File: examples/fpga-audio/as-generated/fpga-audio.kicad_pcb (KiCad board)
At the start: 4 copper layers, 76 x 58 mm, 36 parts, among them J1 3V3 IN, J2 AUDIO OUT, J3 SPI PROG, U1 iCE40UP5K, U2 PCM5102A, U3 AP2112K-1.2, U4 W25Q32JV, X1 12MHz

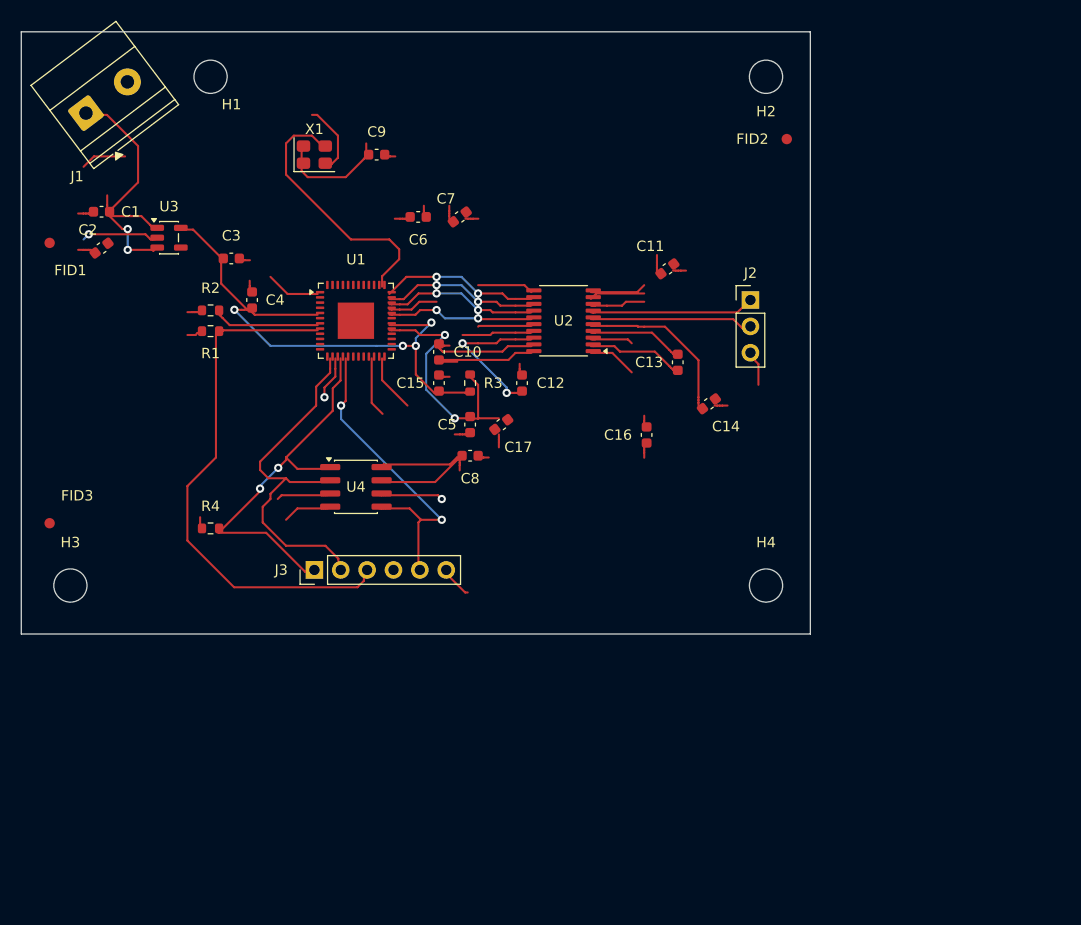
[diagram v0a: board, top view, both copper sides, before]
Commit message: feat(examples): the FPGA board on two layers, and the rim fenced in the generator
The last of the five, and the one that had to be re-floorplanned rather than
converted: a 48-pin QFN, a codec, a boot flash and an oscillator escaped on two
faces. All five examples are now two-layer and gate clean.

What moved, and why:

* the boot flash came up ten millimetres to meet the FPGA's SPI port, the
  configuration header eight west along the bottom edge it serves, and CRESET's
  pull-up now stands between its two ends instead of beside CDONE's. Together
  those took `layout.connection_span` from nine findings - worst 51.5 mm - to
  the four I2S runs at 25.7 mm, which are the two packages' own width.
* the outer ring of the pour is now a router keepout, not just something the
  review reports afterwards. On the widest board in the set the perimeter is
  the emptiest lane there is and the router took it twice, for 20.5 mm of the
  bottom edge and 11.5 mm of the right. Reporting that is `layout.pour_edge_cut`;
  not building it is the generator's job.
* the input rail goes round the screw terminal rather than under its body, the
  core rail's link to its spine is asked for at the width it lands on, and the
  oscillator's bypass takes its supply from the neighbour eight millimetres
  away instead of the flash's bypass fifty-two millimetres away.

What is judged rather than fixed is in `gate.toml` with its measurements: the
two-layer return path on the SPI bus, XSMT's detour - R6 in the corridor was
tried and left five nets with no lane at all - the I2S spans, and two marginal
router artifacts on one escape.

Co-Authored-By: Claude Opus 5 <noreply@anthropic.com>
Claude-Session: https://claude.ai/code/session_01XQE7UkE9WTSMW3oZ3kLeCt
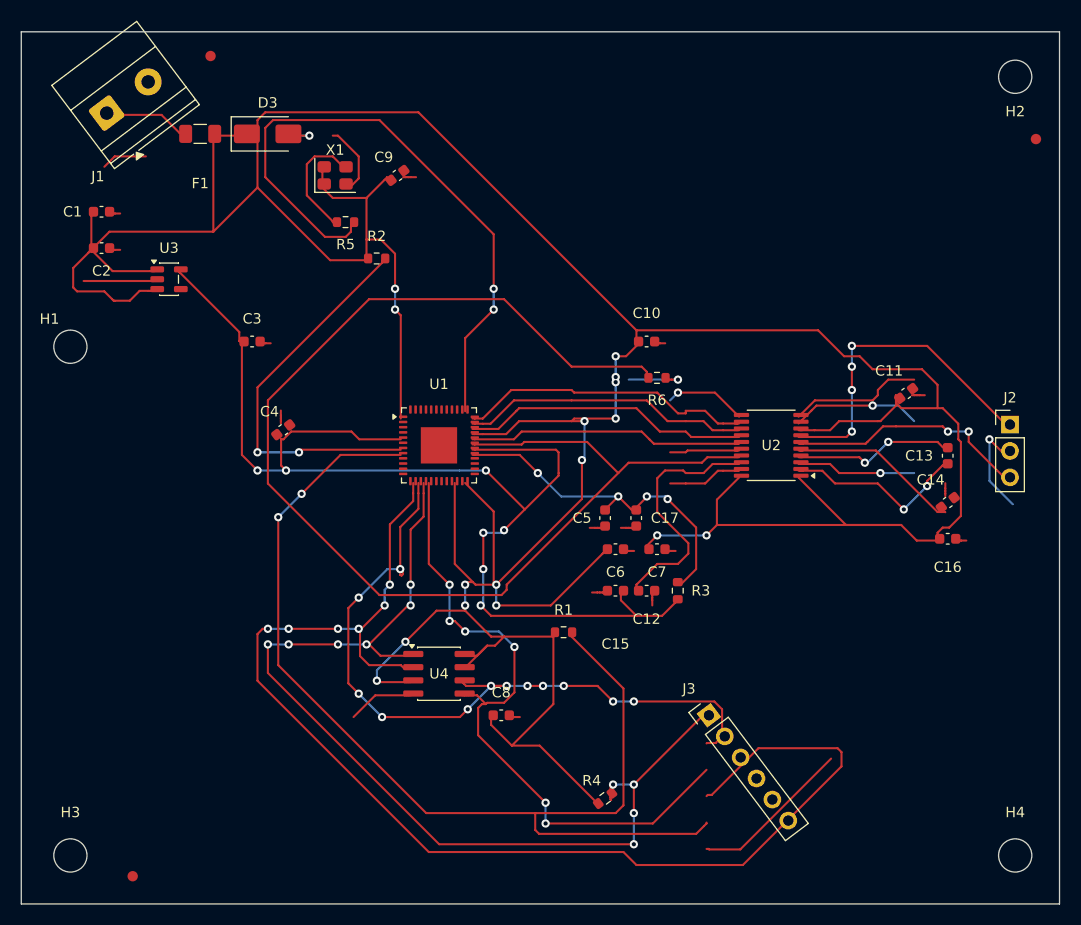
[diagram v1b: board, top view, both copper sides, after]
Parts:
- added C2: 100n, Capacitor_SMD:C_0603_1608Metric, F.Cu at (107.7, 80.8)
- added D3: SMAJ5.0A, Diode_SMD:D_SMA, F.Cu at (123.7, 69.8)
- added R5: 33R, Resistor_SMD:R_0603_1608Metric, F.Cu at (131.2, 78.3)
- added R6: 10k, Resistor_SMD:R_0603_1608Metric, F.Cu at (161.2, 93.3)
- F1: renamed from C2; value 100n -> 500mA; footprint Capacitor_SMD:C_0603_1608Metric -> Fuse:Fuse_1206_3216Metric
- moved R4 46.0 mm to (156.2, 133.8), turned to 37 degrees
- moved R1 44.7 mm to (152.2, 117.8)
- moved J3 40.5 mm to (166.2, 125.8), turned to 37 degrees
- moved C6 37.2 mm to (157.2, 109.8), turned to 0 degrees
- moved C7 37.2 mm to (161.2, 109.8), turned to 0 degrees
- moved H4 35.4 mm to (195.7, 139.3)
- moved FID3 34.9 mm to (110.7, 141.3)
- moved C16 30.7 mm to (189.2, 108.8), turned to 0 degrees
- moved H1 29.3 mm to (104.7, 90.3)
- moved R3 28.3 mm to (163.2, 113.8)
- moved J2 27.7 mm to (195.2, 97.8)
- moved C13 27.5 mm to (189.2, 100.8)
- moved C15 26.2 mm to (157.2, 113.8), turned to 180 degrees
- moved H3 26.0 mm to (104.7, 139.3)
- moved C11 25.9 mm to (185.2, 94.8)
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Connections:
- F1 pad 1: +3V3 -> /VIN
- F1 pad 2: GND -> +3V3
- J1 pad 1: +3V3 -> /VIN
- J2 pad 2: /OUTL -> GND
- J2 pad 3: GND -> /OUTL
- J3 pad 2: /SPI_SO -> /SPI_SCK
- J3 pad 3: /CRESET -> /SPI_SI
- J3 pad 4: /SPI_SCK -> /SPI_SO
- J3 pad 5: /SPI_SI -> /CRESET
- U1 pad 31: unconnected-(U1A-IOT_42b-Pad31) -> /XSMT
- U2 pad 17: +3V3 -> /XSMT
- X1 pad 3: /CLK12 -> /OSC_OUT
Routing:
- net +3V3: track 122.1 -> 412.4 mm, vias 2 -> 16
- net /XSMT: track 0.00 -> 123.2 mm
- net /SPI_SO: track 35.7 -> 122.8 mm, vias 0 -> 6
- net /+1V2: track 54.2 -> 115.0 mm, vias 4 -> 7
- net /SPI_SS: track 37.0 -> 96.2 mm, vias 2 -> 10
- net GND: track 83.4 -> 137.8 mm, vias 1 -> 6
- net /CRESET: track 51.2 -> 105.4 mm, vias 0 -> 2
- net /SPI_SCK: track 34.7 -> 72.6 mm, vias 2 -> 12
- net /CLK12: track 25.6 -> 61.4 mm, vias 0 -> 2
- net /SPI_SI: track 31.4 -> 64.0 mm, vias 2 -> 6
- net /CDONE: track 10.2 -> 37.4 mm, vias 0 -> 2
- net /OUTR: track 15.6 -> 31.8 mm, vias 0 -> 4
- net /I2S_SCK: track 15.3 -> 28.5 mm, vias 2 -> 0
- net /I2S_DIN: track 14.9 -> 27.7 mm, vias 2 -> 0
- net /I2S_BCK: track 15.1 -> 27.8 mm, vias 2 -> 0
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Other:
- board size 76 x 58 mm -> 100 x 84 mm
- copper layers 4 -> 2

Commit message: fix(examples): merge same-net vias a drill cannot place that close
The FPGA board's move to two layers put every layer change on the same
pair of faces, and the search spends a via at each end of a hop. Two hops
that turned round within half a millimetre of each other got a barrel
apiece: 0.5 mm between centres, 0.1 mm between the holes, against the
0.2495 mm the board setup allows. KiCad's DRC reported hole_to_hole; the
gate did not, because the constraint is the board setup's rather than a
rule this toolkit writes.

The pair is one hole on one net whose copper already overlaps. `_uncrowded`
runs after the copper has stopped moving, finds same-net vias closer than
HOLE_TO_HOLE_MM, and puts one via at the centre of every track end the two
were serving - only if that one still reaches all of them. A pad-anchored
via never moves.

Also renumber the two REVIEW.md sections that both came out of the merge
as 26.

Co-Authored-By: Claude Opus 5 <noreply@anthropic.com>
Claude-Session: https://claude.ai/code/session_01XQE7UkE9WTSMW3oZ3kLeCt
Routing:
- net +3V3: vias 16 -> 15
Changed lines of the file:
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@@
   )
   (via
-    (at 163.25 94.75)
+    (at 182 96)
     (size 0.8)
     (drill 0.4)
@@
   )
   (via
-    (at 182 96)
+    (at 182.75 102.5)
     (size 0.8)
     (drill 0.4)
@@
   )
   (via
-    (at 182.75 102.5)
+    (at 193.25 99.25)
     (size 0.8)
     (drill 0.4)
@@
   )
   (via
-    (at 193.25 99.25)
+    (at 163.25 93.5)
     (size 0.8)
     (drill 0.4)
@@
   )
   (via
-    (at 163.25 93.5)
+    (at 163.25 94.75)
     (size 0.8)
     (drill 0.4)
@@
   )
   (via
-    (at 161.25 108.5)
+    (at 166 108.5)
     (size 0.8)
     (drill 0.4)
@@
   )
   (via
-    (at 157.25 93.75)
-    (size 0.8)
-    (drill 0.4)
-    (layers "F.Cu" "B.Cu")
-    (net 3)
-  )
-  (via
-    (at 166 108.5)
+    (at 157.25 97.25)
     (size 0.8)
     (drill 0.4)
@@
   )
   (via
-    (at 157.25 93.25)
+    (at 157.25 93.5)
     (size 0.8)
     (drill 0.4)
@@
   )
   (via
-    (at 157.25 97.25)
+    (at 161.25 108.5)
     (size 0.8)
     (drill 0.4)
@@
   )
   (via
-    (at 183.5 99.5)
+    (at 181.25 101.5)
     (size 0.8)
     (drill 0.4)
@@
   )
   (via
-    (at 181.25 101.5)
+    (at 183.5 99.5)
     (size 0.8)
     (drill 0.4)
@@
   )
   (via
-    (at 145.5 86.75)
+    (at 145.5 84.75)
     (size 0.8)
     (drill 0.4)
@@
   )
   (via
-    (at 145.5 84.75)
+    (at 145.5 86.75)
     (size 0.8)
     (drill 0.4)
@@
   )
   (via
-    (at 124.75 106.75)
+    (at 127 104.5)
     (size 0.8)
     (drill 0.4)
@@
   )
   (via
-    (at 127 104.5)
+    (at 124.75 106.75)
     (size 0.8)
     (drill 0.4)
@@
   )
   (via
-    (at 191.25 98.5)
+    (at 189.25 98.5)
     (size 0.8)
     (drill 0.4)
@@
   )
   (via
-    (at 189.25 98.5)
+    (at 191.25 98.5)
     (size 0.8)
     (drill 0.4)
@@
   )
   (via
-    (at 180 90.25)
+    (at 180 92.25)
     (size 0.8)
     (drill 0.4)
@@
   )
   (via
-    (at 180 94.5)
+    (at 180 90.25)
     (size 0.8)
     (drill 0.4)
@@
   )
   (via
-    (at 180 92.25)
+    (at 180 94.5)
     (size 0.8)
     (drill 0.4)
@@
   )
   (via
-    (at 146.75 123)
+    (at 148.75 123)
     (size 0.8)
     (drill 0.4)
@@
   )
   (via
-    (at 132.5 114.5)
+    (at 132.5 123.75)
     (size 0.8)
     (drill 0.4)
@@
   )
   (via
-    (at 148.75 123)
+    (at 150.25 123)
     (size 0.8)
     (drill 0.4)
@@
   )
   (via
-    (at 159 124.5)
+    (at 157 124.5)
     (size 0.8)
     (drill 0.4)
@@
   )
   (via
-    (at 150.25 123)
+    (at 136.5 111.75)
     (size 0.8)
     (drill 0.4)
@@
   )
   (via
-    (at 132.5 123.75)
+    (at 159 124.5)
     (size 0.8)
     (drill 0.4)
@@
   )
   (via
-    (at 157 124.5)
+    (at 132.5 114.5)
     (size 0.8)
     (drill 0.4)
@@
   )
   (via
-    (at 136.5 111.75)
+    (at 143 125.25)
     (size 0.8)
     (drill 0.4)
@@
   )
   (via
-    (at 145.25 123)
+    (at 146.75 123)
     (size 0.8)
     (drill 0.4)
@@
   )
   (via
-    (at 143 125.25)
+    (at 145.25 123)
     (size 0.8)
     (drill 0.4)
@@
   )
   (via
-    (at 150.5 134.25)
+    (at 141.25 113.25)
     (size 0.8)
     (drill 0.4)
@@
   )
   (via
-    (at 141.25 116.75)
+    (at 150.5 136.25)
     (size 0.8)
     (drill 0.4)
@@
   )
   (via
-    (at 147.5 119.25)
+    (at 142.75 117.75)
     (size 0.8)
     (drill 0.4)
@@
   )
   (via
-    (at 141.25 113.25)
+    (at 150.5 134.25)
     (size 0.8)
     (drill 0.4)
@@
   )
   (via
-    (at 142.75 117.75)
+    (at 141.25 116.75)
     (size 0.8)
     (drill 0.4)
@@
   )
   (via
-    (at 150.5 136.25)
+    (at 147.5 119.25)
     (size 0.8)
     (drill 0.4)
@@
   )
   (via
-    (at 132.5 117.5)
+    (at 135 115.25)
     (size 0.8)
     (drill 0.4)
@@
   )
   (via
-    (at 135 115.25)
+    (at 132.5 117.5)
     (size 0.8)
     (drill 0.4)
@@
   )
   (via
-    (at 159 132.5)
+    (at 159 135.25)
     (size 0.8)
     (drill 0.4)
@@
   )
   (via
-    (at 125.75 119)
+    (at 130.5 119)
     (size 0.8)
     (drill 0.4)
@@
   )
   (via
-    (at 137.5 113.25)
+    (at 123.75 119)
     (size 0.8)
     (drill 0.4)
@@
   )
   (via
-    (at 159 138.25)
+    (at 137.5 115.25)
     (size 0.8)
     (drill 0.4)
@@
   )
   (via
-    (at 137.5 115.25)
+    (at 157 132.5)
     (size 0.8)
     (drill 0.4)
@@
   )
   (via
-    (at 133.25 119)
+    (at 137.5 113.25)
     (size 0.8)
     (drill 0.4)
@@
   )
   (via
-    (at 159 135.25)
+    (at 159 138.25)
     (size 0.8)
     (drill 0.4)
@@
   )
   (via
-    (at 130.5 119)
+    (at 133.25 119)
     (size 0.8)
     (drill 0.4)
@@
   )
   (via
-    (at 123.75 119)
+    (at 125.75 119)
     (size 0.8)
     (drill 0.4)
@@
   )
   (via
-    (at 157 132.5)
+    (at 159 132.5)
     (size 0.8)
     (drill 0.4)
@@
   )
   (via
-    (at 157.5 104.75)
+    (at 160.25 104.75)
     (size 0.8)
     (drill 0.4)
@@
   )
   (via
-    (at 160.25 104.75)
+    (at 157.5 104.75)
     (size 0.8)
     (drill 0.4)

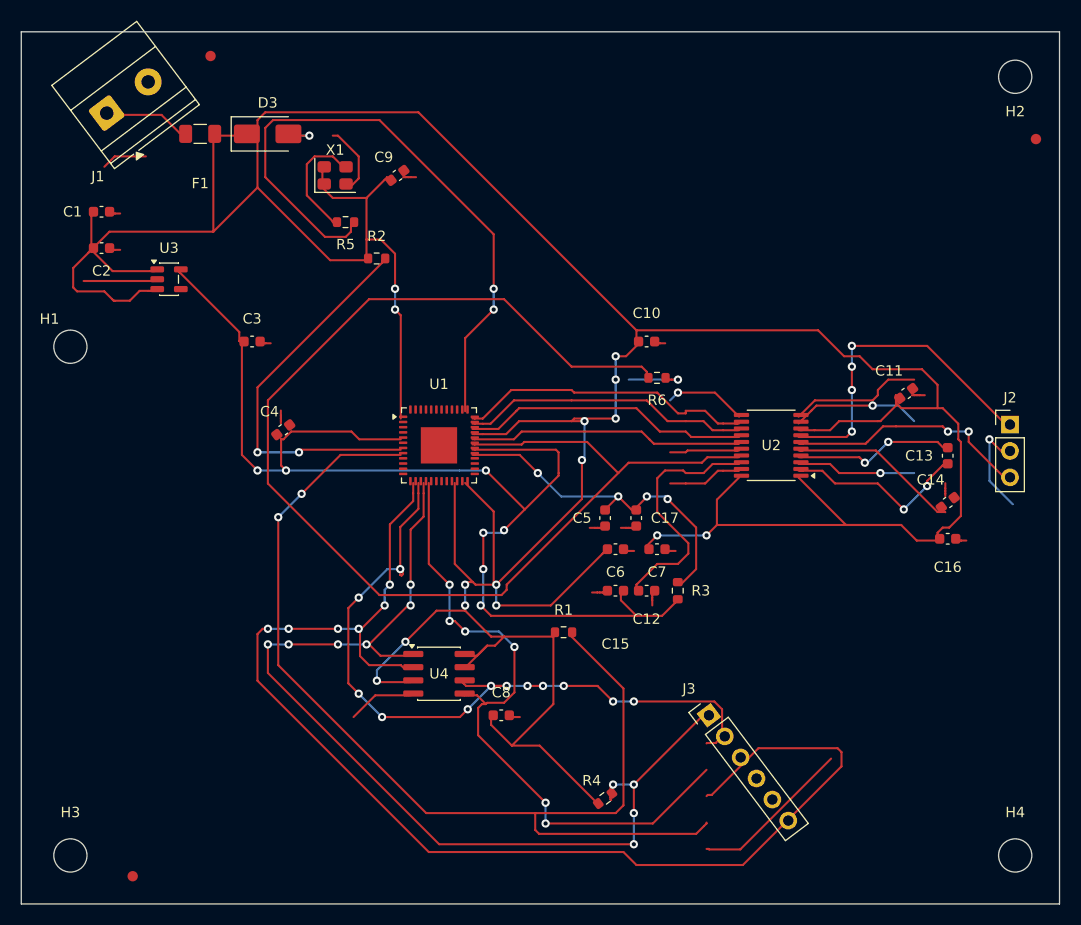
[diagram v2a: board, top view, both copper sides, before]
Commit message: chore(examples): regenerate the FPGA board from a cold route
The board this checkout held came from a warm cache and was clean by
luck: CI routes with an empty cache and no learned rip-up order, found a
different valid solution, and put +3V3 under both headers. With J2 and J3
fenced by body_keepout, the cold route goes round them - no
route.under_package, no pour_edge_cut, DRC clean, gate and contracts pass
on all five boards.

Record the round in REVIEW.md, and state the rule in AGENTS.md: the
copper checked in has to be what a cold route finds, because that is what
the drift check compares against.

Co-Authored-By: Claude Opus 5 <noreply@anthropic.com>
Claude-Session: https://claude.ai/code/session_01XQE7UkE9WTSMW3oZ3kLeCt
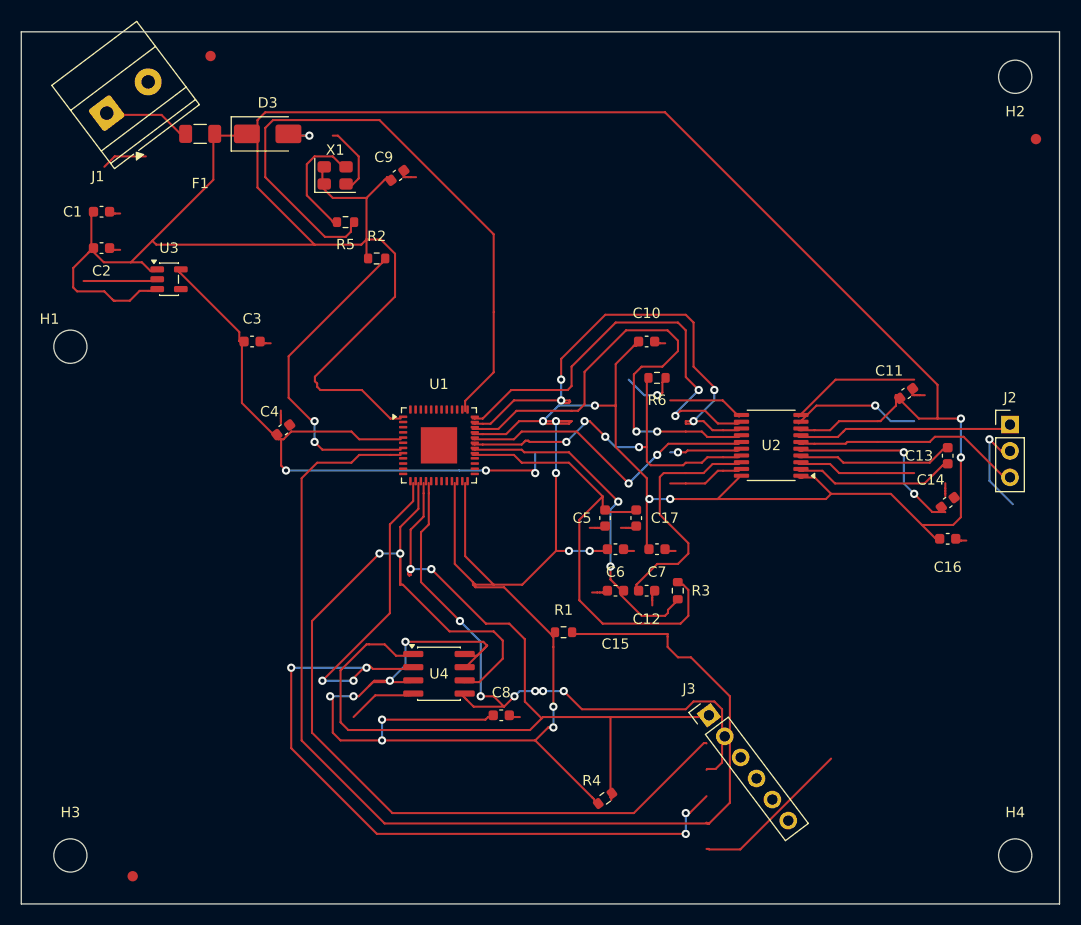
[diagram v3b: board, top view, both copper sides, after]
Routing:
- net /XSMT: track 123.2 -> 36.3 mm, vias 0 -> 4
- net +3V3: track 412.4 -> 460.3 mm, vias 15 -> 18
- net /SPI_SO: track 122.8 -> 93.6 mm
- net /SPI_SCK: track 72.6 -> 98.2 mm, vias 12 -> 2
- net /I2S_BCK: track 27.8 -> 48.2 mm, vias 0 -> 4
- net /I2S_DIN: track 27.7 -> 48.0 mm, vias 0 -> 2
- net /+1V2: track 115.0 -> 94.7 mm, vias 7 -> 5
- net /I2S_SCK: track 28.5 -> 42.3 mm, vias 0 -> 2
- net /OUTR: track 31.8 -> 20.6 mm, vias 4 -> 0
- net /VCCPLL: track 34.6 -> 45.4 mm, vias 4 -> 0
- net /CDONE: track 37.4 -> 31.1 mm
- net /SPI_SS: track 96.2 -> 89.9 mm, vias 10 -> 2
- net /CRESET: track 105.4 -> 110.3 mm, vias 2 -> 0
- net /SPI_SI: track 64.0 -> 60.3 mm
- net /I2S_LRCK: track 26.5 -> 29.7 mm, vias 0 -> 2
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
